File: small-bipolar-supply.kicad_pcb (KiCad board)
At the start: 2 copper layers, 25.5 x 25 mm, 23 parts, among them J1 USB_C_Receptacle_PowerOnly_6P, J10 Conn_01x01, J2 Conn_01x02, J3 Conn_01x02, J4 Conn_01x02, J7 Conn_01x02, J8 Conn_01x02, J9 Conn_01x01, U1 LM2776

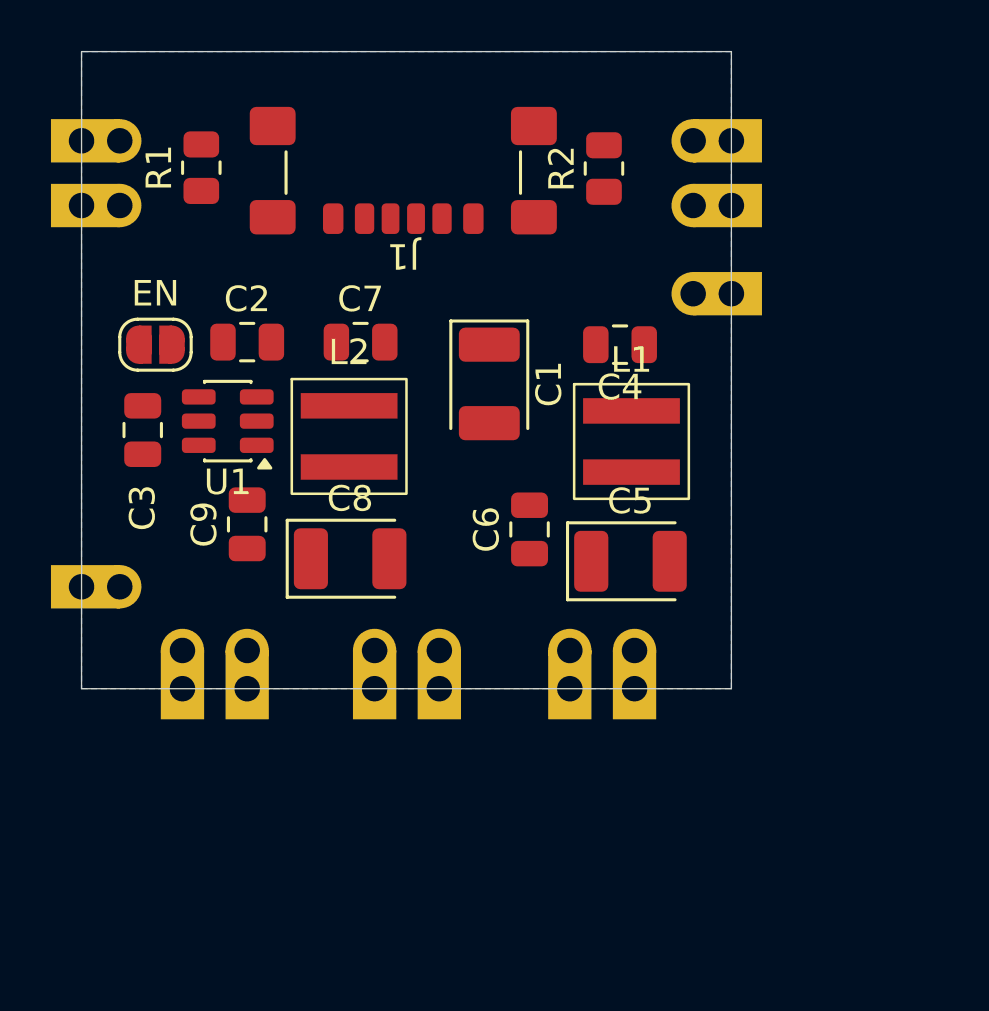
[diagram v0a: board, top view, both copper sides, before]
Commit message: chore: PCB pin spacing optimised for breadboard use
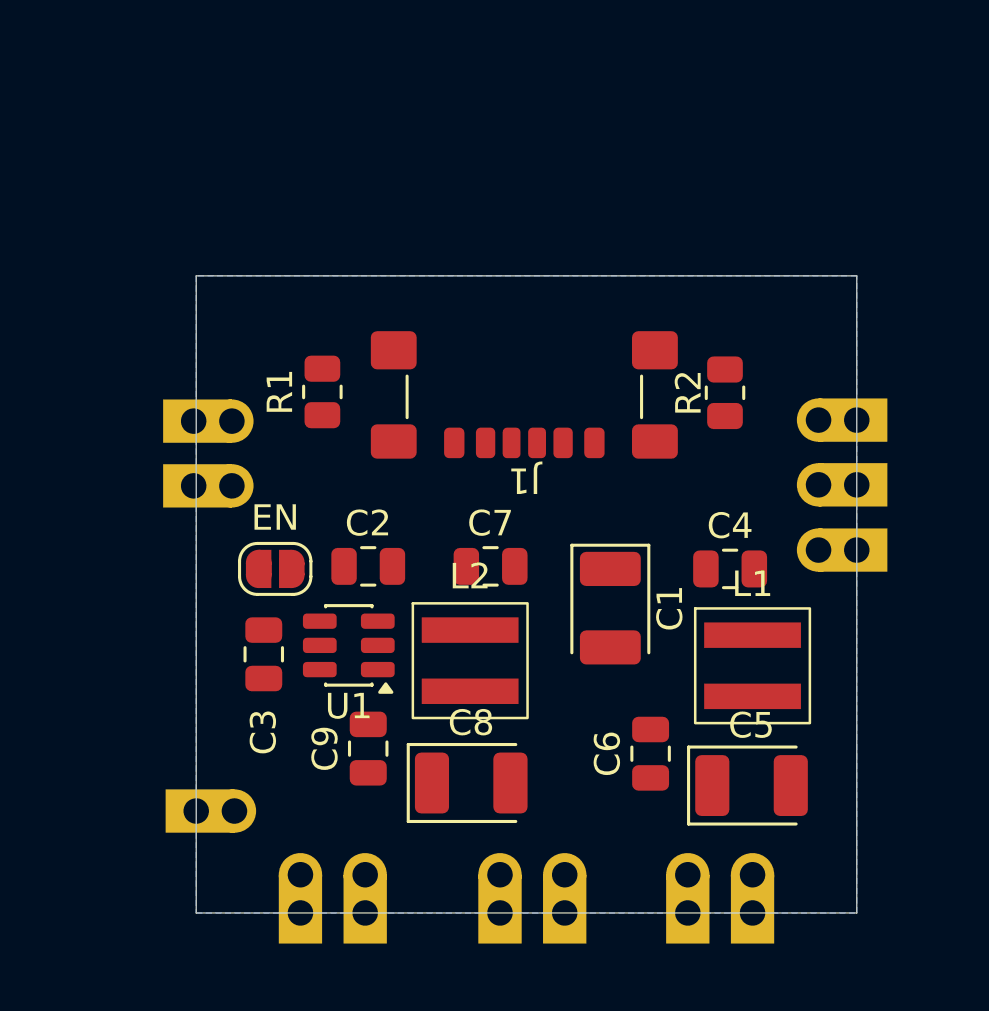
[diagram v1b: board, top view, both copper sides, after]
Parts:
- moved J3 12.0 mm to (113.9, 54.0)
- moved J2 11.8 mm to (87.9, 56.5)
- moved J10 11.2 mm to (113.9, 59.1)
- moved C7 10.2 mm to (99.5, 59.7)
- moved J4 10.1 mm to (102.4, 73.3)
- moved C1 10.0 mm to (104.2, 61.3)
- moved C2 10.0 mm to (94.8, 59.7)
- moved C8 10.0 mm to (98.8, 68.2)
- moved L1 10.0 mm to (109.8, 63.6)
- moved R2 10.0 mm to (108.8, 52.9)
- moved C3 10.0 mm to (90.7, 63.1)
- moved C5 10.0 mm to (109.8, 68.3)
- moved C6 10.0 mm to (105.8, 67.0)
- moved C9 10.0 mm to (94.8, 66.8)
- moved J1 10.0 mm to (100.9, 51.8)
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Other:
- board size 25.5 x 25 mm -> 25.9 x 25 mm
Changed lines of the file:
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@@
 	(footprint "Package_TO_SOT_SMD:SOT-23-6"
 		(layer "F.Cu")
-		(at 89.2375 54 180)
+		(at 93.9875 62.8 180)
 		(descr "SOT, 6 Pin (JEDEC MO-178 Var AB https://www.jedec.org/document_search?search_api_views_fulltext=MO-178)")
 		(tags "SOT TO_SOT_SMD")
@@
 	(footprint "small-bipolar-supply:SRP4020"
 		(layer "F.Cu")
-		(at 94 54.6)
+		(at 98.75 63.4)
 		(property "Reference" "L2"
 			(at 0 -3.3 0)
@@
 	(footprint "Capacitor_Tantalum_SMD:CP_EIA-3528-12_Kemet-T"
 		(layer "F.Cu")
-		(at 94.04 59.4)
+		(at 98.79 68.2)
 		(descr "Tantalum Capacitor SMD Kemet-T (3528-12 Metric), IPC-7352 nominal, (Body size from: http://www.kemet.com/Lists/ProductCatalog/Attachments/253/KEM_TC101_STD.pdf)")
 		(tags "capacitor tantalum")
@@
 	(footprint "Capacitor_SMD:C_0805_2012Metric"
 		(layer "F.Cu")
-		(at 90 58.05 90)
+		(at 94.75 66.85 90)
 		(descr "Capacitor SMD 0805 (2012 Metric), square (rectangular) end terminal, IPC-7351 nominal, (Body size source: IPC-SM-782 page 76, https://www.pcb-3d.com/wordpress/wp-content/uploads/ipc-sm-782a_amendment_1_and_2.pdf, https://docs.google.com/spreadsheets/d/1BsfQQcO9C6DZCsRaXUlFlo91Tg2WpOkGARC1WS5S8t0/edit?usp=sharing)")
 		(tags "capacitor")
@@
 	(footprint "small-bipolar-supply:SRP4020"
 		(layer "F.Cu")
-		(at 105.08 54.8)
+		(at 109.83 63.6)
 		(property "Reference" "L1"
 			(at 0 -3.2 0)
@@
 	(footprint "Connector_USB:USB_C_Receptacle_GCT_USB4135-GF-A_6P_TopMnt_Horizontal"
 		(layer "F.Cu")
-		(at 96.125 43.0225 180)
+		(at 100.875 51.8225 180)
 		(descr "USB Type C Receptacle, GCT, power-only, 6P, top mounted, horizontal, 3A: https://gct.co/files/drawings/usb4135.pdf")
 		(tags "USB C Type-C Receptacle SMD USB Power-only Charging-only 6P 6C USB4135-GF-A")
@@
 	(footprint "Capacitor_SMD:C_0805_2012Metric"
 		(layer "F.Cu")
-		(at 104.63 51 180)
+		(at 108.95 59.8)
 		(descr "Capacitor SMD 0805 (2012 Metric), square (rectangular) end terminal, IPC-7351 nominal, (Body size source: IPC-SM-782 page 76, https://www.pcb-3d.com/wordpress/wp-content/uploads/ipc-sm-782a_amendment_1_and_2.pdf, https://docs.google.com/spreadsheets/d/1BsfQQcO9C6DZCsRaXUlFlo91Tg2WpOkGARC1WS5S8t0/edit?usp=sharing)")
 		(tags "capacitor")
@@
 		(duplicate_pad_numbers_are_jumpers no)
 		(fp_line
-			(start -0.261252 0.735)
-			(end 0.261252 0.735)
+			(start -0.261252 -0.735)
+			(end 0.261252 -0.735)
 			(stroke
 				(width 0.12)
@@
 		)
 		(fp_line
-			(start -0.261252 -0.735)
-			(end 0.261252 -0.735)
+			(start -0.261252 0.735)
+			(end 0.261252 0.735)
 			(stroke
 				(width 0.12)
@@
 		)
 		(pad "1" smd roundrect
-			(at -0.95 0 180)
+			(at -0.95 0)
 			(size 1 1.45)
 			(layers "F.Cu" "F.Mask" "F.Paste")
@@
 		)
 		(pad "2" smd roundrect
-			(at 0.95 0 180)
+			(at 0.95 0)
 			(size 1 1.45)
 			(layers "F.Cu" "F.Mask" "F.Paste")
@@
 	(footprint "small-bipolar-supply:castellated_2_P2.54mm"
 		(layer "F.Cu")
-		(at 109 43.04)
+		(at 113.92 54)
 		(descr "Through hole straight pin header, 1x02, 2.54mm pitch, single row")
 		(tags "Through hole pin header THT 1x02 2.54mm single row")
@@
 		(sheetname "/")
 		(sheetfile "small-bipolar-supply.kicad_sch")
-		(units
-			(unit
-				(name "A")
-				(pins "1" "2")
-			)
-		)
 		(attr through_hole)
 		(duplicate_pad_numbers_are_jumpers no)
 		(fp_rect
-			(start -3 -1.77)
-			(end 1.77 4.32)
+			(start -2.5 -1)
+			(end 1.5 3.5)
 			(stroke
 				(width 0.05)
@@
 	(footprint "Capacitor_Tantalum_SMD:CP_EIA-3528-12_Kemet-T"
 		(layer "F.Cu")
-		(at 99.5 52.54 -90)
+		(at 104.25 61.34 -90)
 		(descr "Tantalum Capacitor SMD Kemet-T (3528-12 Metric), IPC-7352 nominal, (Body size from: http://www.kemet.com/Lists/ProductCatalog/Attachments/253/KEM_TC101_STD.pdf)")
 		(tags "capacitor tantalum")
@@
 	(footprint "small-bipolar-supply:castellated_1_P2.54mm"
 		(layer "F.Cu")
-		(at 109 49.04)
+		(at 113.92 59.1)
 		(descr "Through hole straight pin header, 1x02, 2.54mm pitch, single row")
 		(tags "Through hole pin header THT 1x02 2.54mm single row")
@@
 		(sheetname "/")
 		(sheetfile "small-bipolar-supply.kicad_sch")
-		(units
-			(unit
-				(name "A")
-				(pins "1")
-			)
-		)
 		(attr through_hole)
 		(duplicate_pad_numbers_are_jumpers no)
 		(fp_rect
-			(start -3 -1.5)
-			(end 1.77 1.275)
+			(start -2.5 -1)
+			(end 1.5 1)
 			(stroke
 				(width 0.05)
@@
 	(footprint "Resistor_SMD:R_0805_2012Metric"
 		(layer "F.Cu")
-		(at 104 44.0875 90)
+		(at 108.75 52.8875 90)
 		(descr "Resistor SMD 0805 (2012 Metric), square (rectangular) end terminal, IPC-7351 nominal, (Body size source: IPC-SM-782 page 72, https://www.pcb-3d.com/wordpress/wp-content/uploads/ipc-sm-782a_amendment_1_and_2.pdf)")
 		(tags "resistor")
 		(property "Reference" "R2"
-			(at 0 -1.65 90)
+			(at 0 -1.42 90)
 			(layer "F.SilkS")
 			(effects
@@
 	(footprint "Capacitor_SMD:C_0805_2012Metric"
 		(layer "F.Cu")
-		(at 94.45 50.9)
+		(at 99.55 59.7)
 		(descr "Capacitor SMD 0805 (2012 Metric), square (rectangular) end terminal, IPC-7351 nominal, (Body size source: IPC-SM-782 page 76, https://www.pcb-3d.com/wordpress/wp-content/uploads/ipc-sm-782a_amendment_1_and_2.pdf, https://docs.google.com/spreadsheets/d/1BsfQQcO9C6DZCsRaXUlFlo91Tg2WpOkGARC1WS5S8t0/edit?usp=sharing)")
 		(tags "capacitor")
@@
 	(footprint "Capacitor_SMD:C_0805_2012Metric"
 		(layer "F.Cu")
-		(at 90 50.9)
+		(at 94.75 59.7)
 		(descr "Capacitor SMD 0805 (2012 Metric), square (rectangular) end terminal, IPC-7351 nominal, (Body size source: IPC-SM-782 page 76, https://www.pcb-3d.com/wordpress/wp-content/uploads/ipc-sm-782a_amendment_1_and_2.pdf, https://docs.google.com/spreadsheets/d/1BsfQQcO9C6DZCsRaXUlFlo91Tg2WpOkGARC1WS5S8t0/edit?usp=sharing)")
 		(tags "capacitor")
@@
 	(footprint "Jumper:SolderJumper-2_P1.3mm_Open_RoundedPad1.0x1.5mm"
 		(layer "F.Cu")
-		(at 86.4 51)
+		(at 91.1 59.8)
 		(descr "SMD Solder Jumper, 1x1.5mm, rounded Pads, 0.3mm gap, open")
 		(tags "solder jumper open")
@@
 	(footprint "small-bipolar-supply:castellated_2_P2.54mm"
 		(layer "F.Cu")
-		(at 89.96 64.5 -90)
+		(at 94.59 73.3 -90)
 		(descr "Through hole straight pin header, 1x02, 2.54mm pitch, single row")
 		(tags "Through hole pin header THT 1x02 2.54mm single row")
@@
 	(footprint "small-bipolar-supply:castellated_1_P2.54mm"
 		(layer "F.Cu")
-		(at 83.5 60.46 180)
+		(at 88 69.26 180)
 		(descr "Through hole straight pin header, 1x02, 2.54mm pitch, single row")
 		(tags "Through hole pin header THT 1x02 2.54mm single row")
@@
 	(footprint "small-bipolar-supply:castellated_2_P2.54mm"
 		(layer "F.Cu")
-		(at 83.5 45.5 180)
+		(at 87.9 56.5 180)
 		(descr "Through hole straight pin header, 1x02, 2.54mm pitch, single row")
 		(tags "Through hole pin header THT 1x02 2.54mm single row")
@@
 		(sheetname "/")
 		(sheetfile "small-bipolar-supply.kicad_sch")
-		(units
-			(unit
-				(name "A")
-				(pins "1" "2")
-			)
-		)
 		(attr through_hole)
 		(duplicate_pad_numbers_are_jumpers no)
 		(fp_rect
-			(start -3 -1.77)
-			(end 1.77 4.32)
+			(start -2.5 -1)
+			(end 1.5 3.5)
 			(stroke
 				(width 0.05)
@@
 	(footprint "small-bipolar-supply:castellated_2_P2.54mm"
 		(layer "F.Cu")
-		(at 105.16 64.5 -90)
+		(at 109.79 73.3 -90)
 		(descr "Through hole straight pin header, 1x02, 2.54mm pitch, single row")
 		(tags "Through hole pin header THT 1x02 2.54mm single row")
@@
 	(footprint "Resistor_SMD:R_0805_2012Metric"
 		(layer "F.Cu")
-		(at 88.2 44.055 90)
+		(at 92.95 52.855 90)
 		(descr "Resistor SMD 0805 (2012 Metric), square (rectangular) end terminal, IPC-7351 nominal, (Body size source: IPC-SM-782 page 72, https://www.pcb-3d.com/wordpress/wp-content/uploads/ipc-sm-782a_amendment_1_and_2.pdf)")
 		(tags "resistor")
@@
 	(footprint "Capacitor_SMD:C_0805_2012Metric"
 		(layer "F.Cu")
-		(at 85.9 54.35 90)
+		(at 90.65 63.15 90)
 		(descr "Capacitor SMD 0805 (2012 Metric), square (rectangular) end terminal, IPC-7351 nominal, (Body size source: IPC-SM-782 page 76, https://www.pcb-3d.com/wordpress/wp-content/uploads/ipc-sm-782a_amendment_1_and_2.pdf, https://docs.google.com/spreadsheets/d/1BsfQQcO9C6DZCsRaXUlFlo91Tg2WpOkGARC1WS5S8t0/edit?usp=sharing)")
 		(tags "capacitor")
@@
 	(footprint "Capacitor_Tantalum_SMD:CP_EIA-3528-12_Kemet-T"
 		(layer "F.Cu")
-		(at 105.04 59.5)
+		(at 109.79 68.3)
 		(descr "Tantalum Capacitor SMD Kemet-T (3528-12 Metric), IPC-7352 nominal, (Body size from: http://www.kemet.com/Lists/ProductCatalog/Attachments/253/KEM_TC101_STD.pdf)")
 		(tags "capacitor tantalum")
@@
 	(footprint "Capacitor_SMD:C_0805_2012Metric"
 		(layer "F.Cu")
-		(at 101.08 58.25 90)
+		(at 105.83 67.05 90)
 		(descr "Capacitor SMD 0805 (2012 Metric), square (rectangular) end terminal, IPC-7351 nominal, (Body size source: IPC-SM-782 page 76, https://www.pcb-3d.com/wordpress/wp-content/uploads/ipc-sm-782a_amendment_1_and_2.pdf, https://docs.google.com/spreadsheets/d/1BsfQQcO9C6DZCsRaXUlFlo91Tg2WpOkGARC1WS5S8t0/edit?usp=sharing)")
 		(tags "capacitor")
@@
 	(footprint "small-bipolar-supply:castellated_2_P2.54mm"
 		(layer "F.Cu")
-		(at 97.5 64.5 -90)
+		(at 102.42 73.3 -90)
 		(descr "Through hole straight pin header, 1x02, 2.54mm pitch, single row")
 		(tags "Through hole pin header THT 1x02 2.54mm single row")
@@
 		)
 		(fp_text user "${REFERENCE}"
-			(at 0 1.27 0)
+			(at 0 1.44 0)
 			(layer "F.Fab")
 			(effects
@@
 	)
 	(gr_rect
-		(start 83.5 39.5)
-		(end 109 64.5)
+		(start 88 48.3)
+		(end 113.92 73.3)
 		(stroke
 			(width 0.05)
@@
 		(polygon
 			(pts
-				(xy 109 39.5) (xy 83.5 39.5) (xy 83.5 64.5) (xy 109 64.5)
+				(xy 113.92 48.3) (xy 88 48.3) (xy 88 73.3) (xy 113.92 73.3)
 			)
 		)
 	)
 	(group ""
+		(members "3756573b-ed5b-45c3-b41b-79f1439409c7" "5bfd246e-3dad-4949-b18b-d2e0ae085978")
+	)
+	(group ""

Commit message: feat/done: tuned component layout and silkscreen
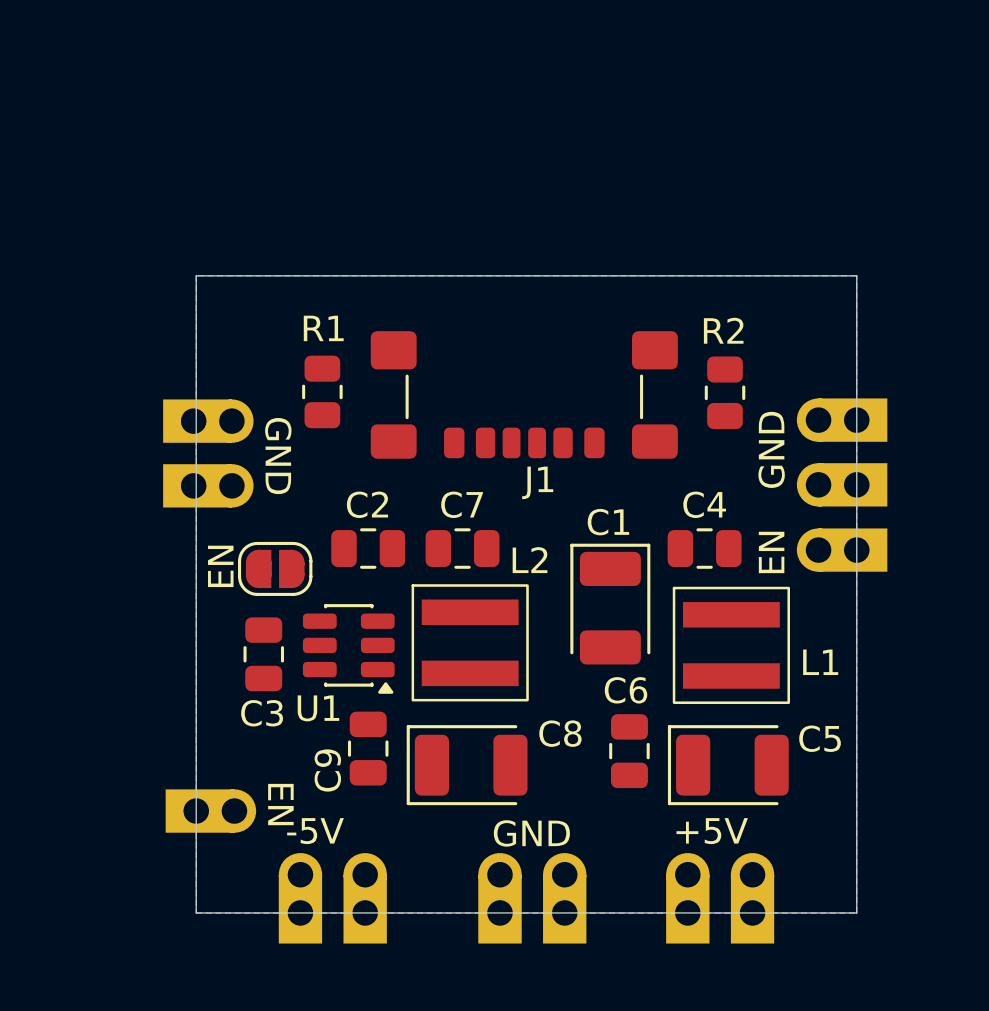
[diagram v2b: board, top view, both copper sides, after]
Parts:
- moved C7 1.30 mm to (98.5, 59.0)
- moved C4 1.28 mm to (108.0, 59.0)
- moved L1 1.15 mm to (109.0, 62.8)
- moved C5 1.10 mm to (109.0, 67.5)
- moved C6 0.84 mm to (105.0, 67.0)
- moved C2 0.70 mm to (94.8, 59.0)
- moved C8 0.70 mm to (98.8, 67.5)
- moved L2 0.70 mm to (98.8, 62.7)
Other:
- board text added: "+5V"
- board text added: "-5V"
- board text added: "EN"
- board text added: "GND"
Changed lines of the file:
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@@
 		(tags "SOT TO_SOT_SMD")
 		(property "Reference" "U1"
-			(at 0 -2.4 0)
+			(at 1.1875 -2.5 0)
 			(layer "F.SilkS")
 			(effects
@@
 	(footprint "small-bipolar-supply:SRP4020"
 		(layer "F.Cu")
-		(at 98.75 63.4)
+		(at 98.75 62.7)
 		(property "Reference" "L2"
-			(at 0 -3.3 0)
+			(at 2.35 -3.2 0)
 			(unlocked yes)
 			(layer "F.SilkS")
@@
 	(footprint "Capacitor_Tantalum_SMD:CP_EIA-3528-12_Kemet-T"
 		(layer "F.Cu")
-		(at 98.79 68.2)
+		(at 98.79 67.5)
 		(descr "Tantalum Capacitor SMD Kemet-T (3528-12 Metric), IPC-7352 nominal, (Body size from: http://www.kemet.com/Lists/ProductCatalog/Attachments/253/KEM_TC101_STD.pdf)")
 		(tags "capacitor tantalum")
 		(property "Reference" "C8"
-			(at 0 -2.35 0)
+			(at 3.51 -1.2 0)
 			(layer "F.SilkS")
 			(effects
@@
 		(tags "capacitor")
 		(property "Reference" "C9"
-			(at 0 -1.68 90)
+			(at -0.85 -1.55 270)
 			(layer "F.SilkS")
 			(effects
@@
 	(footprint "small-bipolar-supply:SRP4020"
 		(layer "F.Cu")
-		(at 109.83 63.6)
+		(at 109 62.8)
 		(property "Reference" "L1"
-			(at 0 -3.2 0)
+			(at 3.5 0.7 0)
 			(unlocked yes)
 			(layer "F.SilkS")
@@
 		(tags "USB C Type-C Receptacle SMD USB Power-only Charging-only 6P 6C USB4135-GF-A")
 		(property "Reference" "J1"
-			(at 0 -4.5 180)
+			(at -0.625 -4.5 0)
 			(unlocked yes)
 			(layer "F.SilkS")
@@
 	(footprint "Capacitor_SMD:C_0805_2012Metric"
 		(layer "F.Cu")
-		(at 108.95 59.8)
+		(at 107.95 59)
 		(descr "Capacitor SMD 0805 (2012 Metric), square (rectangular) end terminal, IPC-7351 nominal, (Body size source: IPC-SM-782 page 76, https://www.pcb-3d.com/wordpress/wp-content/uploads/ipc-sm-782a_amendment_1_and_2.pdf, https://docs.google.com/spreadsheets/d/1BsfQQcO9C6DZCsRaXUlFlo91Tg2WpOkGARC1WS5S8t0/edit?usp=sharing)")
 		(tags "capacitor")
@@
 		(tags "capacitor tantalum")
 		(property "Reference" "C1"
-			(at 0 -2.35 90)
+			(at -3.34 0.05 180)
 			(layer "F.SilkS")
 			(effects
@@
 		(tags "resistor")
 		(property "Reference" "R2"
-			(at 0 -1.42 90)
+			(at 2.3875 -0.05 0)
 			(layer "F.SilkS")
 			(effects
@@
 	(footprint "Capacitor_SMD:C_0805_2012Metric"
 		(layer "F.Cu")
-		(at 99.55 59.7)
+		(at 98.45 59)
 		(descr "Capacitor SMD 0805 (2012 Metric), square (rectangular) end terminal, IPC-7351 nominal, (Body size source: IPC-SM-782 page 76, https://www.pcb-3d.com/wordpress/wp-content/uploads/ipc-sm-782a_amendment_1_and_2.pdf, https://docs.google.com/spreadsheets/d/1BsfQQcO9C6DZCsRaXUlFlo91Tg2WpOkGARC1WS5S8t0/edit?usp=sharing)")
 		(tags "capacitor")
@@
 	(footprint "Capacitor_SMD:C_0805_2012Metric"
 		(layer "F.Cu")
-		(at 94.75 59.7)
+		(at 94.75 59)
 		(descr "Capacitor SMD 0805 (2012 Metric), square (rectangular) end terminal, IPC-7351 nominal, (Body size source: IPC-SM-782 page 76, https://www.pcb-3d.com/wordpress/wp-content/uploads/ipc-sm-782a_amendment_1_and_2.pdf, https://docs.google.com/spreadsheets/d/1BsfQQcO9C6DZCsRaXUlFlo91Tg2WpOkGARC1WS5S8t0/edit?usp=sharing)")
 		(tags "capacitor")
@@
 		)
 		(property "SILK" "EN"
-			(at 0 -2 0)
+			(at -2.1 -0.1 90)
 			(unlocked yes)
 			(layer "F.SilkS")
@@
 		(tags "resistor")
 		(property "Reference" "R1"
-			(at 0 -1.65 90)
+			(at 2.455 0.05 0)
 			(layer "F.SilkS")
 			(effects
@@
 		(tags "capacitor")
 		(property "Reference" "C3"
-			(at -3.05 0 90)
+			(at -2.35 -0.05 180)
 			(layer "F.SilkS")
 			(effects
@@
 	(footprint "Capacitor_Tantalum_SMD:CP_EIA-3528-12_Kemet-T"
 		(layer "F.Cu")
-		(at 109.79 68.3)
+		(at 109.04 67.5)
 		(descr "Tantalum Capacitor SMD Kemet-T (3528-12 Metric), IPC-7352 nominal, (Body size from: http://www.kemet.com/Lists/ProductCatalog/Attachments/253/KEM_TC101_STD.pdf)")
 		(tags "capacitor tantalum")
 		(property "Reference" "C5"
-			(at 0 -2.35 0)
+			(at 3.46 -1 0)
 			(layer "F.SilkS")
 			(effects
@@
 	(footprint "Capacitor_SMD:C_0805_2012Metric"
 		(layer "F.Cu")
-		(at 105.83 67.05 90)
+		(at 105 66.95 90)
 		(descr "Capacitor SMD 0805 (2012 Metric), square (rectangular) end terminal, IPC-7351 nominal, (Body size source: IPC-SM-782 page 76, https://www.pcb-3d.com/wordpress/wp-content/uploads/ipc-sm-782a_amendment_1_and_2.pdf, https://docs.google.com/spreadsheets/d/1BsfQQcO9C6DZCsRaXUlFlo91Tg2WpOkGARC1WS5S8t0/edit?usp=sharing)")
 		(tags "capacitor")
 		(property "Reference" "C6"
-			(at 0 -1.68 90)
+			(at 2.35 -0.13 180)
 			(layer "F.SilkS")
 			(effects
@@
 		(layer "Edge.Cuts")
 	)
+	(gr_text "-5V\n"
+		(at 91.5 70.7 0)
+		(layer "F.SilkS")
+		(effects
+			(font
+				(size 1 1)
+				(thickness 0.1)
+			)
+			(justify left bottom)
+		)
+	)
+	(gr_text "GND\n"
+		(at 99.6 70.8 0)
+		(layer "F.SilkS")
+		(effects
+			(font
+				(size 1 1)
+				(thickness 0.1)
+			)
+			(justify left bottom)
+		)
+	)
+	(gr_text "+5V\n"
+		(at 106.7 70.7 0)
+		(layer "F.SilkS")
+		(effects
+			(font
+				(size 1 1)
+				(thickness 0.1)
+			)
+			(justify left bottom)
+		)
+	)
+	(gr_text "GND\n"
+		(at 111.2 56.7 90)
+		(layer "F.SilkS")
+		(effects
+			(font
+				(size 1 1)
+				(thickness 0.1)
+			)
+			(justify left bottom)
+		)
+	)
+	(gr_text "EN"
+		(at 111.2 60.1 90)
+		(layer "F.SilkS")
+		(effects
+			(font
+				(size 1 1)
+				(thickness 0.1)
+			)
+			(justify left bottom)
+		)
+	)
+	(gr_text "GND\n"
+		(at 90.6 53.8 270)
+		(layer "F.SilkS")
+		(effects
+			(font
+				(size 1 1)
+				(thickness 0.1)
+			)
+			(justify left bottom)
+		)
+	)
+	(gr_text "EN"
+		(at 90.7 68.1 270)
+		(layer "F.SilkS")
+		(effects
+			(font
+				(size 1 1)
+				(thickness 0.1)
+			)
+			(justify left bottom)
+		)
+	)
 	(zone
